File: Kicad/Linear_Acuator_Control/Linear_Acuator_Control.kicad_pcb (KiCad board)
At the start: 2 copper layers, 89.5 x 64.8 mm, 10 parts, among them K1 RT42xAxx, K3 RT42xAxx, Q1 IRLZ44N, Q2 IRLZ44N, U1 ESP32-S3-DevKitC

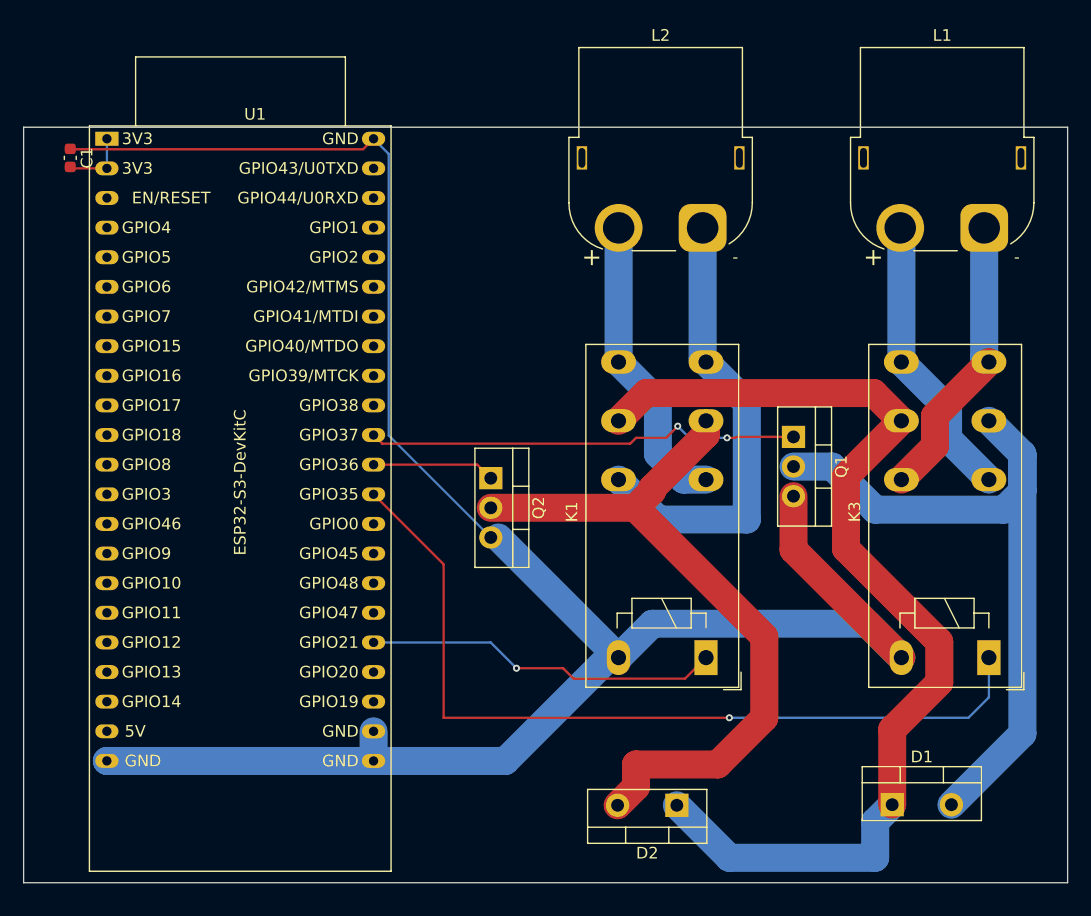
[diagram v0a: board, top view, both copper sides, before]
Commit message: changed to male XT60 connector
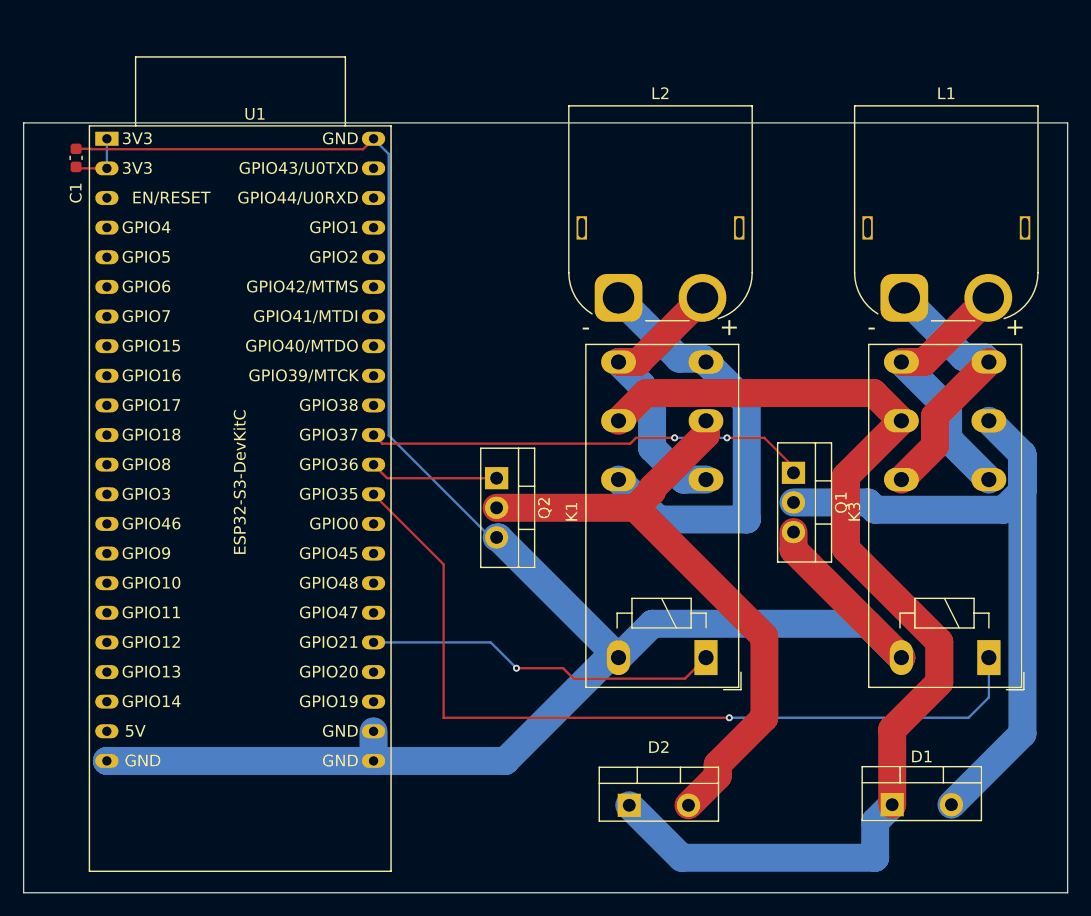
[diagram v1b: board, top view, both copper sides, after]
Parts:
- L1, L2: footprint Connector_AMASS:AMASS_XT60PW-F_1x02_P7.20mm_Horizontal -> Connector_AMASS:AMASS_XT60PW-M_1x02_P7.20mm_Horizontal
- moved L2 9.38 mm to (114.5, 54.0)
- moved L1 9.11 mm to (139.0, 54.0)
- moved D2 4.08 mm to (115.4, 97.5), turned to 0 degrees
- moved Q1 3.08 mm to (129.5, 69.0)
- moved C1 0.50 mm to (68.0, 42.0)
- moved Q2 0.50 mm to (104.0, 69.5)
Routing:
- net Net-(D2-A): track 61.6 -> 54.4 mm
- net +24V: track 90.1 -> 94.2 mm
- net GND: track 174.3 -> 170.8 mm
- net Net-(L1-Pin_1): track 24.9 -> 22.7 mm
- net Net-(L2-Pin_1): track 39.0 -> 37.1 mm
- net Net-(L1-Pin_2): track 24.7 -> 22.9 mm
- net Net-(L2-Pin_2): track 25.3 -> 23.8 mm
- net Net-(D1-A): track 61.6 -> 60.3 mm
- net Speed L2: track 10.5 -> 11.0 mm
- net +3V3: track 5.73 -> 5.23 mm
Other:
- board size 89.5 x 64.8 mm -> 89.5 x 66 mm

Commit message: Power input, minor rearranging
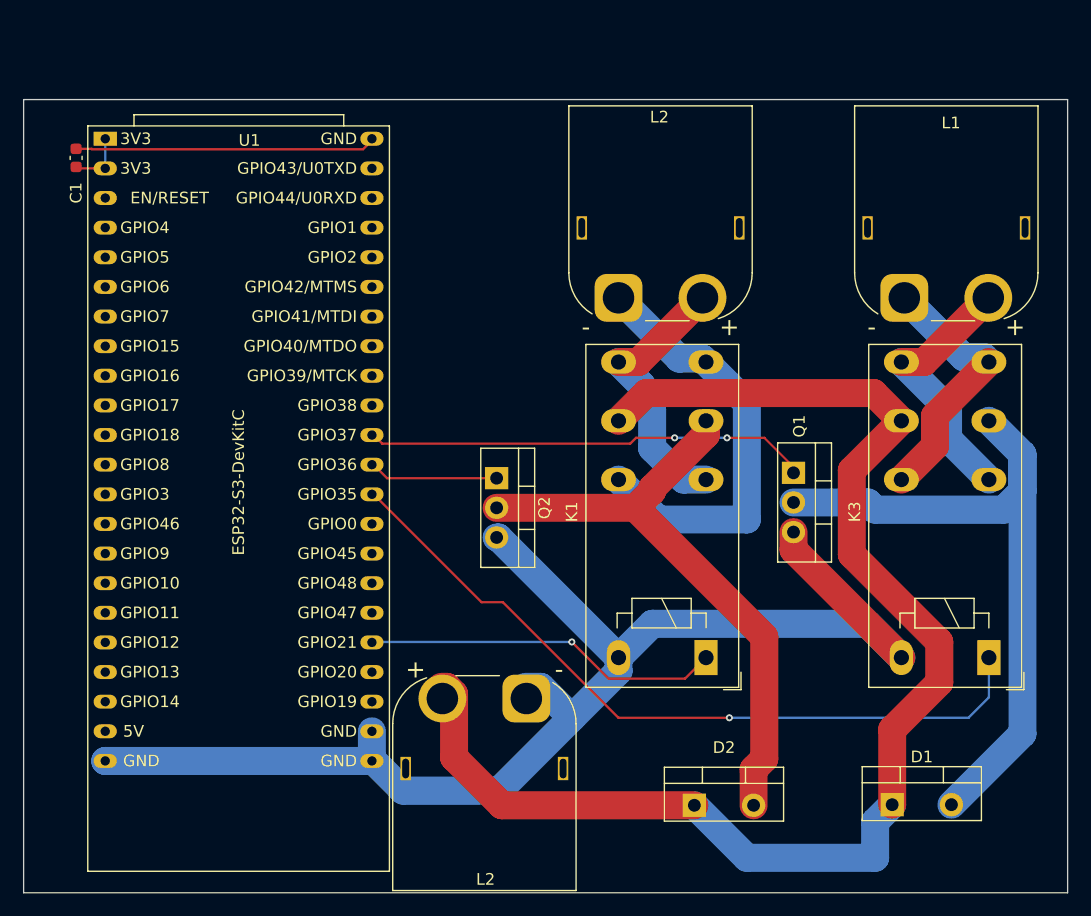
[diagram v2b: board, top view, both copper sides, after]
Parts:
- added L2: 24v input, Connector_AMASS:AMASS_XT60PW-M_1x02_P7.20mm_Horizontal, F.Cu at (106.6, 88.3)
- moved D2 5.58 mm to (121.0, 97.5)
- moved U1 0.14 mm to (70.5, 40.4)
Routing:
- net GND: track 170.8 -> 141.6 mm
- net +24V: track 94.2 -> 117.3 mm
- net Dir L1: track 72.5 -> 65.0 mm
- net Net-(D2-A): track 54.4 -> 52.1 mm
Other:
- board size 89.5 x 66 mm -> 89.5 x 68 mm

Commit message: Minor Fix
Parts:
- renumbered L2 to L3
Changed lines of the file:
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@@
 		(descr "Connector XT60 Horizontal PCB Female, https://www.tme.eu/Document/b13629717d44ae038681dba08d18c0b6/XT60PW-M.pdf")
 		(tags "RC Connector XT60")
-		(property "Reference" "L2"
+		(property "Reference" "L3"
 			(at 3.5 -15.5 0)
 			(layer "F.SilkS")
